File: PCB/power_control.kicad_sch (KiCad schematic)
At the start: 10 parts

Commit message: task: alert on Basic-library alternatives during JLC part matching (#33)
* task: alert on Basic-library alternatives during JLC part matching

JLC's "Extended" library carries a per-unique-part setup fee on top of
unit price; "Basic" doesn't. That fee doesn't amortize well on a board
with many distinct low-quantity parts -- confirmed the hard way: our
first real JLCPCB assembly quote came back at $333.84 vs PCBWay's
~$190 for the same order, and all 33 of our matched parts were
Extended.

jlc_match.py now does a secondary search for a same-value/same-package
Basic-library part whenever the real match lands on Extended, and
flags it in the report (new BasicAlt column + a Status alert) rather
than silently leaving it. On the current board this surfaces 11
plausible Basic-library swaps (common resistor/cap values, and the
generic 1N4148W diode and 2N7002 MOSFET, which are industry-standard
parts many brands stock identically).

This is alert-only, same as the rest of this script -- it doesn't
touch the schematic. Spot-checked 4 of the 11 suggestions directly
against JLC's catalog to confirm value/package actually match, not
just a keyword hit.

Co-Authored-By: Claude Sonnet 5 <noreply@anthropic.com>

* fix: two correctness bugs in Basic-library alternative matching

1. find_basic_alternative() trusted the raw keyword-search hit without
   verifying the candidate's actual value -- JLC's fuzzy full-text search
   can return a wrong-value part that just shares digits (e.g. searching
   "100 0402" surfaced a 1kΩ resistor, EIA code "1001", as a false match
   for a 100Ω part). Now parses and compares the actual numeric value
   (with unit) before accepting a candidate; falls back to exact
   model-name matching for non-numeric values (generic diode/transistor
   part families like "1N4148W", "2N7002").

2. The new value parser's regex required the unit to be the first
   character of the string, but JLC resistor descriptions carry a
   Chinese prefix ("厚膜电阻 10kΩ ±1%" = "thi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
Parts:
- C_DBNC1: LCSC C131394 -> C1525; MF Yageo -> Samsung Electro-Mechanics; Manufacturer_Part_Number CC0402KRX7R9BB104 -> CL05B104KO5NNNC
- D_OR1, D_OR2: LCSC C83528 -> C81598; MF Diodes Incorporated -> ST(Semtech); Manufacturer_Part_Number 1N4148W-7-F -> 1N4148W
- Q_LATCH1: LCSC C16338 -> C8545; MF onsemi -> Jiangsu Changjing Electronics Technology Co., Ltd.; Manufacturer_Part_Number 2N7002LT1G -> 2N7002
- R_BTN_PU1, R_GATE1, R_PWR_SENSE1: LCSC C60491 -> C25741; MF Yageo -> UNI-ROYAL(Uniroyal Elec); Manufacturer_Part_Number RC0402FR-07100KL -> 0402WGF1003TCE
- R_LATCH_G1: LCSC C60490 -> C25744; MF Yageo -> UNI-ROYAL(Uniroyal Elec); Manufacturer_Part_Number RC0402FR-0710KL -> 0402WGF1002TCE
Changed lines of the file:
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@@
 			)
 		)
-		(property "MF" "Yageo"
-			(at 0 0 0)
-			(hide yes)
-			(show_name no)
-			(do_not_autoplace no)
-			(effects
-				(font
-					(size 1.27 1.27)
-				)
-			)
-		)
-		(property "Manufacturer_Part_Number" "CC0402KRX7R9BB104"
-			(at 0 0 0)
-			(hide yes)
-			(show_name no)
-			(do_not_autoplace no)
-			(effects
-				(font
-					(size 1.27 1.27)
-				)
-			)
-		)
-		(property "LCSC" "C131394"
+		(property "MF" "Samsung Electro-Mechanics"
+			(at 0 0 0)
+			(hide yes)
+			(show_name no)
+			(do_not_autoplace no)
+			(effects
+				(font
+					(size 1.27 1.27)
+				)
+			)
+		)
+		(property "Manufacturer_Part_Number" "CL05B104KO5NNNC"
+			(at 0 0 0)
+			(hide yes)
+			(show_name no)
+			(do_not_autoplace no)
+			(effects
+				(font
+					(size 1.27 1.27)
+				)
+			)
+		)
+		(property "LCSC" "C1525"
 			(at 0 0 0)
 			(hide yes)
@@
 			)
 		)
-		(property "MF" "Diodes Incorporated"
-			(at 0 0 0)
-			(hide yes)
-			(show_name no)
-			(do_not_autoplace no)
-			(effects
-				(font
-					(size 1.27 1.27)
-				)
-			)
-		)
-		(property "Manufacturer_Part_Number" "1N4148W-7-F"
-			(at 0 0 0)
-			(hide yes)
-			(show_name no)
-			(do_not_autoplace no)
-			(effects
-				(font
-					(size 1.27 1.27)
-				)
-			)
-		)
-		(property "LCSC" "C83528"
+		(property "MF" "ST(Semtech)"
+			(at 0 0 0)
+			(hide yes)
+			(show_name no)
+			(do_not_autoplace no)
+			(effects
+				(font
+					(size 1.27 1.27)
+				)
+			)
+		)
+		(property "Manufacturer_Part_Number" "1N4148W"
+			(at 0 0 0)
+			(hide yes)
+			(show_name no)
+			(do_not_autoplace no)
+			(effects
+				(font
+					(size 1.27 1.27)
+				)
+			)
+		)
+		(property "LCSC" "C81598"
 			(at 0 0 0)
 			(hide yes)
@@
 			)
 		)
-		(property "MF" "Yageo"
-			(at 0 0 0)
-			(hide yes)
-			(show_name no)
-			(do_not_autoplace no)
-			(effects
-				(font
-					(size 1.27 1.27)
-				)
-			)
-		)
-		(property "Manufacturer_Part_Number" "RC0402FR-07100KL"
-			(at 0 0 0)
-			(hide yes)
-			(show_name no)
-			(do_not_autoplace no)
-			(effects
-				(font
-					(size 1.27 1.27)
-				)
-			)
-		)
-		(property "LCSC" "C60491"
+		(property "MF" "UNI-ROYAL(Uniroyal Elec)"
+			(at 0 0 0)
+			(hide yes)
+			(show_name no)
+			(do_not_autoplace no)
+			(effects
+				(font
+					(size 1.27 1.27)
+				)
+			)
+		)
+		(property "Manufacturer_Part_Number" "0402WGF1003TCE"
+			(at 0 0 0)
+			(hide yes)
+			(show_name no)
+			(do_not_autoplace no)
+			(effects
+				(font
+					(size 1.27 1.27)
+				)
+			)
+		)
+		(property "LCSC" "C25741"
 			(at 0 0 0)
 			(hide yes)
@@
 			)
 		)
-		(property "MF" "Yageo"
-			(at 0 0 0)
-			(hide yes)
-			(show_name no)
-			(do_not_autoplace no)
-			(effects
-				(font
-					(size 1.27 1.27)
-				)
-			)
-		)
-		(property "Manufacturer_Part_Number" "RC0402FR-0710KL"
-			(at 0 0 0)
-			(hide yes)
-			(show_name no)
-			(do_not_autoplace no)
-			(effects
-				(font
-					(size 1.27 1.27)
-				)
-			)
-		)
-		(property "LCSC" "C60490"
+		(property "MF" "UNI-ROYAL(Uniroyal Elec)"
+			(at 0 0 0)
+			(hide yes)
+			(show_name no)
+			(do_not_autoplace no)
+			(effects
+				(font
+					(size 1.27 1.27)
+				)
+			)
+		)
+		(property "Manufacturer_Part_Number" "0402WGF1002TCE"
+			(at 0 0 0)
+			(hide yes)
+			(show_name no)
+			(do_not_autoplace no)
+			(effects
+				(font
+					(size 1.27 1.27)
+				)
+			)
+		)
+		(property "LCSC" "C25744"
 			(at 0 0 0)
 			(hide yes)
@@
 			)
 		)
-		(property "MF" "Yageo"
-			(at 0 0 0)
-			(hide yes)
-			(show_name no)
-			(do_not_autoplace no)
-			(effects
-				(font
-					(size 1.27 1.27)
-				)
-			)
-		)
-		(property "Manufacturer_Part_Number" "RC0402FR-07100KL"
-			(at 0 0 0)
-			(hide yes)
-			(show_name no)
-			(do_not_autoplace no)
-			(effects
-				(font
-					(size 1.27 1.27)
-				)
-			)
-		)
-		(property "LCSC" "C60491"
+		(property "MF" "UNI-ROYAL(Uniroyal Elec)"
+			(at 0 0 0)
+			(hide yes)
+			(show_name no)
+			(do_not_autoplace no)
+			(effects
+				(font
+					(size 1.27 1.27)
+				)
+			)
+		)
+		(property "Manufacturer_Part_Number" "0402WGF1003TCE"
+			(at 0 0 0)
+			(hide yes)
+			(show_name no)
+			(do_not_autoplace no)
+			(effects
+				(font
+					(size 1.27 1.27)
+				)
+			)
+		)
+		(property "LCSC" "C25741"
 			(at 0 0 0)
 			(hide yes)
@@
 			)
 		)
-		(property "MF" "Diodes Incorporated"
-			(at 0 0 0)
-			(hide yes)
-			(show_name no)
-			(do_not_autoplace no)
-			(effects
-				(font
-					(size 1.27 1.27)
-				)
-			)
-		)
-		(property "Manufacturer_Part_Number" "1N4148W-7-F"
-			(at 0 0 0)
-			(hide yes)
-			(show_name no)
-			(do_not_autoplace no)
-			(effects
-				(font
-					(size 1.27 1.27)
-				)
-			)
-		)
-		(property "LCSC" "C83528"
+		(property "MF" "ST(Semtech)"
+			(at 0 0 0)
+			(hide yes)
+			(show_name no)
+			(do_not_autoplace no)
+			(effects
+				(font
+					(size 1.27 1.27)
+				)
+			)
+		)
+		(property "Manufacturer_Part_Number" "1N4148W"
+			(at 0 0 0)
+			(hide yes)
+			(show_name no)
+			(do_not_autoplace no)
+			(effects
+				(font
+					(size 1.27 1.27)
+				)
+			)
+		)
+		(property "LCSC" "C81598"
 			(at 0 0 0)
 			(hide yes)
@@
 			)
 		)
-		(property "MF" "onsemi"
-			(at 0 0 0)
-			(hide yes)
-			(show_name no)
-			(do_not_autoplace no)
-			(effects
-				(font
-					(size 1.27 1.27)
-				)
-			)
-		)
-		(property "Manufacturer_Part_Number" "2N7002LT1G"
-			(at 0 0 0)
-			(hide yes)
-			(show_name no)
-			(do_not_autoplace no)
-			(effects
-				(font
-					(size 1.27 1.27)
-				)
-			)
-		)
-		(property "LCSC" "C16338"
+		(property "MF" "Jiangsu Changjing Electronics Technology Co., Ltd."
+			(at 0 0 0)
+			(hide yes)
+			(show_name no)
+			(do_not_autoplace no)
+			(effects
+				(font
+					(size 1.27 1.27)
+				)
+			)
+		)
+		(property "Manufacturer_Part_Number" "2N7002"
+			(at 0 0 0)
+			(hide yes)
+			(show_name no)
+			(do_not_autoplace no)
+			(effects
+				(font
+					(size 1.27 1.27)
+				)
+			)
+		)
+		(property "LCSC" "C8545"
 			(at 0 0 0)
 			(hide yes)
@@
 			)
 		)
-		(property "MF" "Yageo"
-			(at 0 0 0)
-			(hide yes)
-			(show_name no)
-			(do_not_autoplace no)
-			(effects
-				(font
-					(size 1.27 1.27)
-				)
-			)
-		)
-		(property "Manufacturer_Part_Number" "RC0402FR-07100KL"
-			(at 0 0 0)
-			(hide yes)
-			(show_name no)
-			(do_not_autoplace no)
-			(effects
-				(font
-					(size 1.27 1.27)
-				)
-			)
-		)
-		(property "LCSC" "C60491"
-			(at 0 0 0)
-			(hide yes)
+		(property "MF" "UNI-ROYAL(Uniroyal Elec)"
+			(at 0 0 0)
+			(hide yes)
+			(show_name no)
+			(do_not_autoplace no)
+			(effects
+				(font
+					(size 1.27 1.27)
+				)
+			)
+		)
+		(property "Manufacturer_Part_Number" "0402WGF1003TCE"
+			(at 0 0 0)
+			(hide yes)
+			(show_name no)
+			(do_not_autoplace no)
+			(effects
+				(font
+					(size 1.27 1.27)
+				)
+			)
+		)
+		(property "LCSC" "C25741"
+			(at 0 0 0)
+			(hide yes)

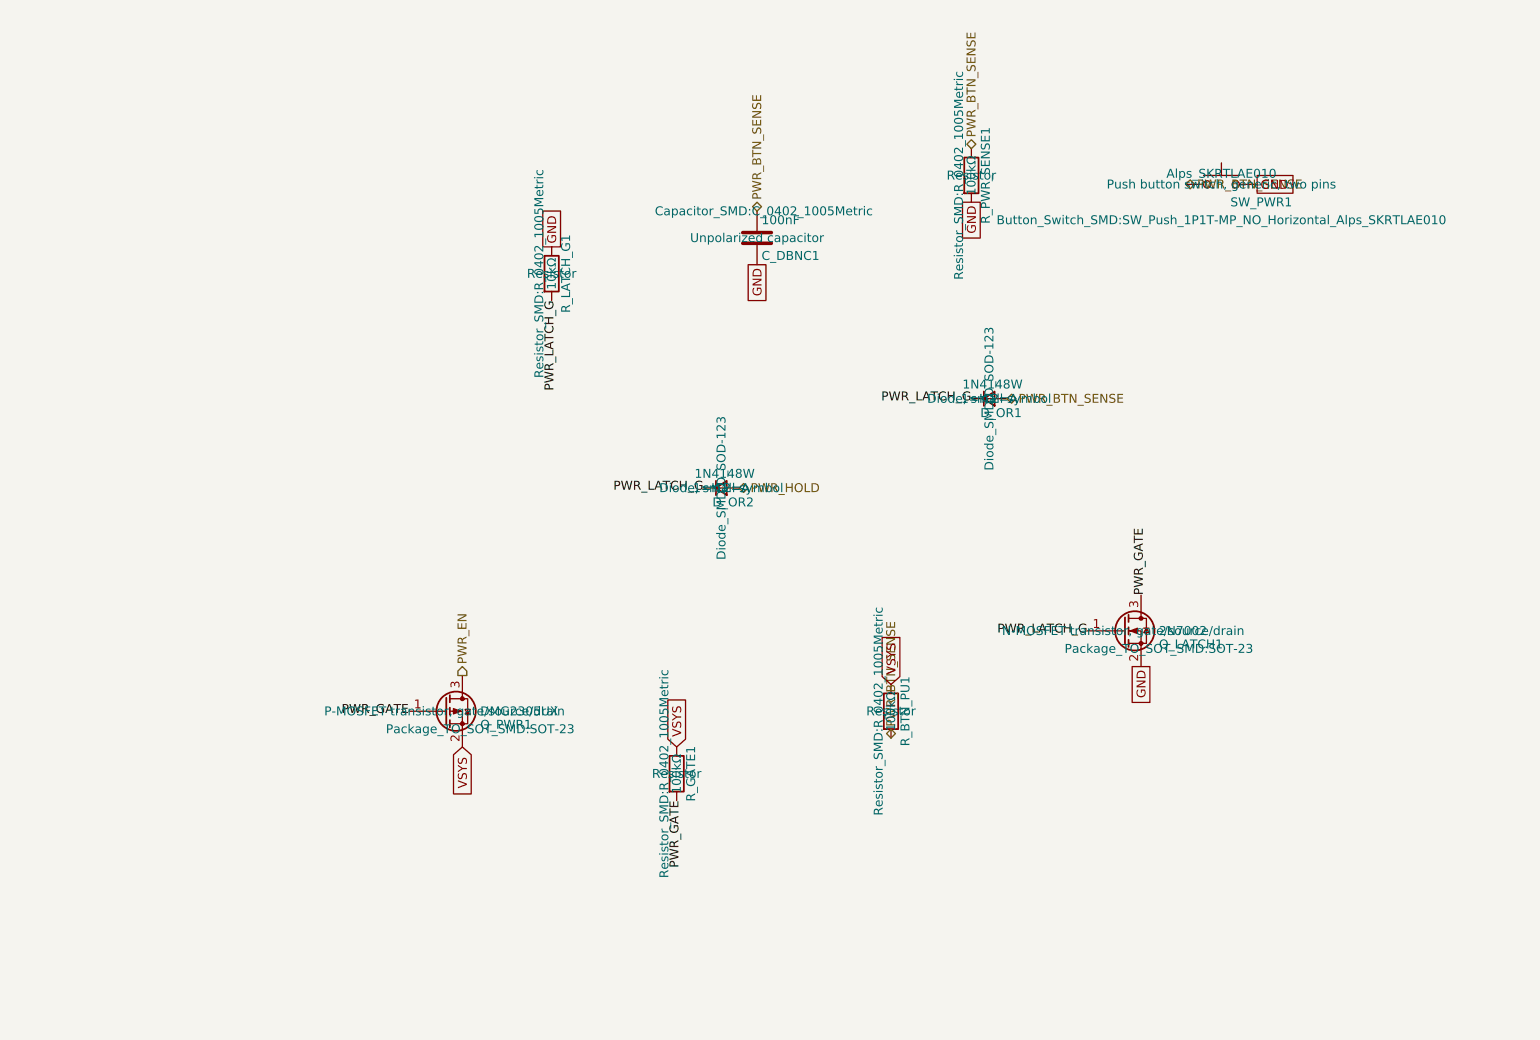
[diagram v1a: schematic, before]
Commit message: fix: power-latch false-trigger, RGB LED footprint regression, JST connector clarity (#56)
Power latch: battery-only bring-up showed the board powering on immediately
with no button press, because PWR_BTN_SENSE's resistor divider idled at
~VSYS/2, forward-biasing D_OR1's anode directly. Adds a transistor inverter
(R_INV_BASE1 / Q_INV1 / R_INV_PU1) so only an actual button press can
forward-bias D_OR1; removes the now-unnecessary R_PWR_SENSE1. New parts
matched to JLCPCB Basic-library equivalents. PCB layout, diagrams, and
power_control_layout docs updated to match.

RGB LED: fixes a regression where D_RGB1's Footprint had reverted to the
stale large SK6812 PLCC4 part in both the cached lib_symbols default and the
instance override, instead of the custom SK6812MINI-E-012 footprint that
PCBWay's earlier assembly rejection required.

JST battery connector: PCBWay's assembly mounted BT1 vertically instead of
horizontal. Confirmed via two independent distributor sources (JLC + LCSC)
that the specified MPN (S2B-PH-K(LF)(SN)) is genuinely a right-angle/
horizontal part, so this was an assembly-side error, not a design bug.
Made the Value/Description fields explicitly say RIGHT-ANGLE / HORIZONTAL
so it's unambiguous in the exported BOM this time.

Co-authored-by: Claude Sonnet 5 <noreply@anthropic.com>
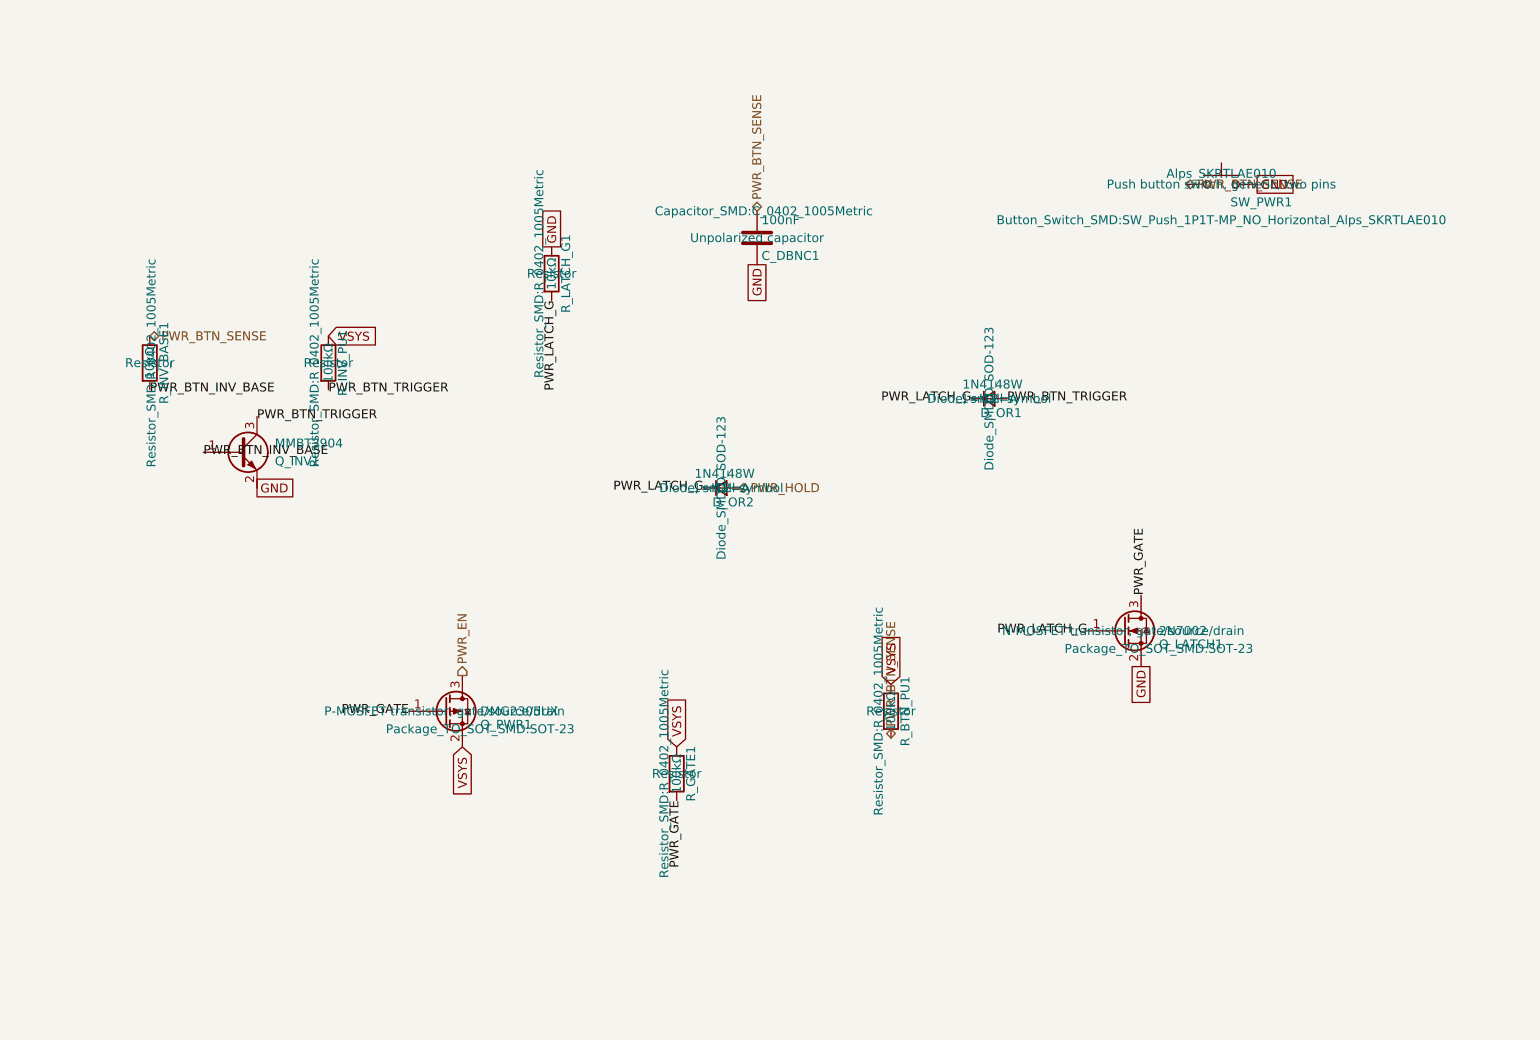
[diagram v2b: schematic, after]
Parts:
- removed R_PWR_SENSE1: 100kΩ, Resistor_SMD:R_0402_1005Metric, symbol Device:R
- added Q_INV1: MMBT3904, Package_TO_SOT_SMD:SOT-23, symbol Transistor_BJT:Q_NPN_BEC
- added R_INV_BASE1: 10kΩ, Resistor_SMD:R_0402_1005Metric, symbol Device:R
- added R_INV_PU1: 100kΩ, Resistor_SMD:R_0402_1005Metric, symbol Device:R
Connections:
- net GND: now also Q_INV1.2 (E)
- net PWR_BTN_SENSE: now also R_INV_BASE1.1; no longer D_OR1.2 (A)
- net VSYS: now also R_INV_PU1.1
- new net PWR_BTN_INV_BASE: Q_INV1.1 (B), R_INV_BASE1.2
- new net PWR_BTN_TRIGGER: D_OR1.2 (A), Q_INV1.3 (C), R_INV_PU1.2
